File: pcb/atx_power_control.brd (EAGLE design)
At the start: 86 x 70 mm, 57 parts, among them IC2 REG1117, IC3 STM32F042F4, IC4 MY_7905DT, J1 ATX24RH, SW1 324_SW, SW2 324_SW, SW3 324_SW, SW4 324_SW, U2 USBC_16P

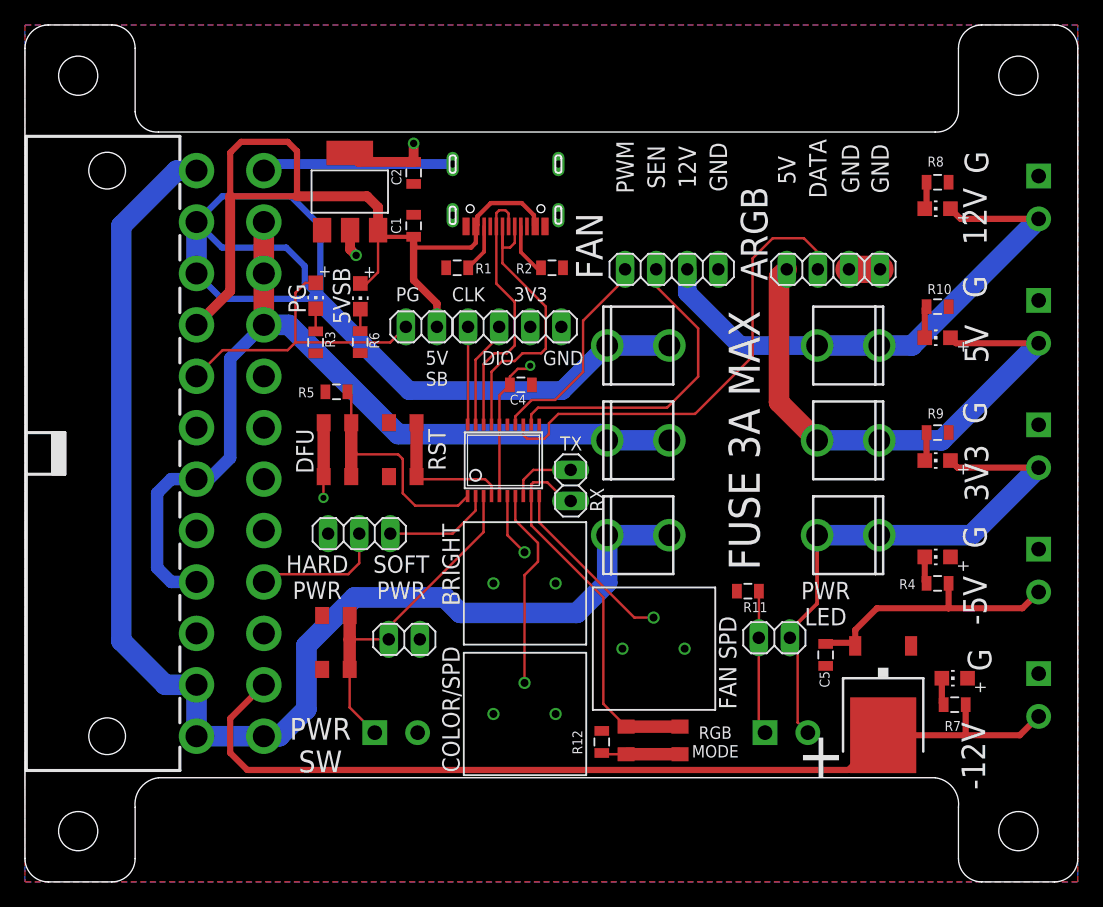
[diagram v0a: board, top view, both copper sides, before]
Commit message: removed pot and added buttons and header
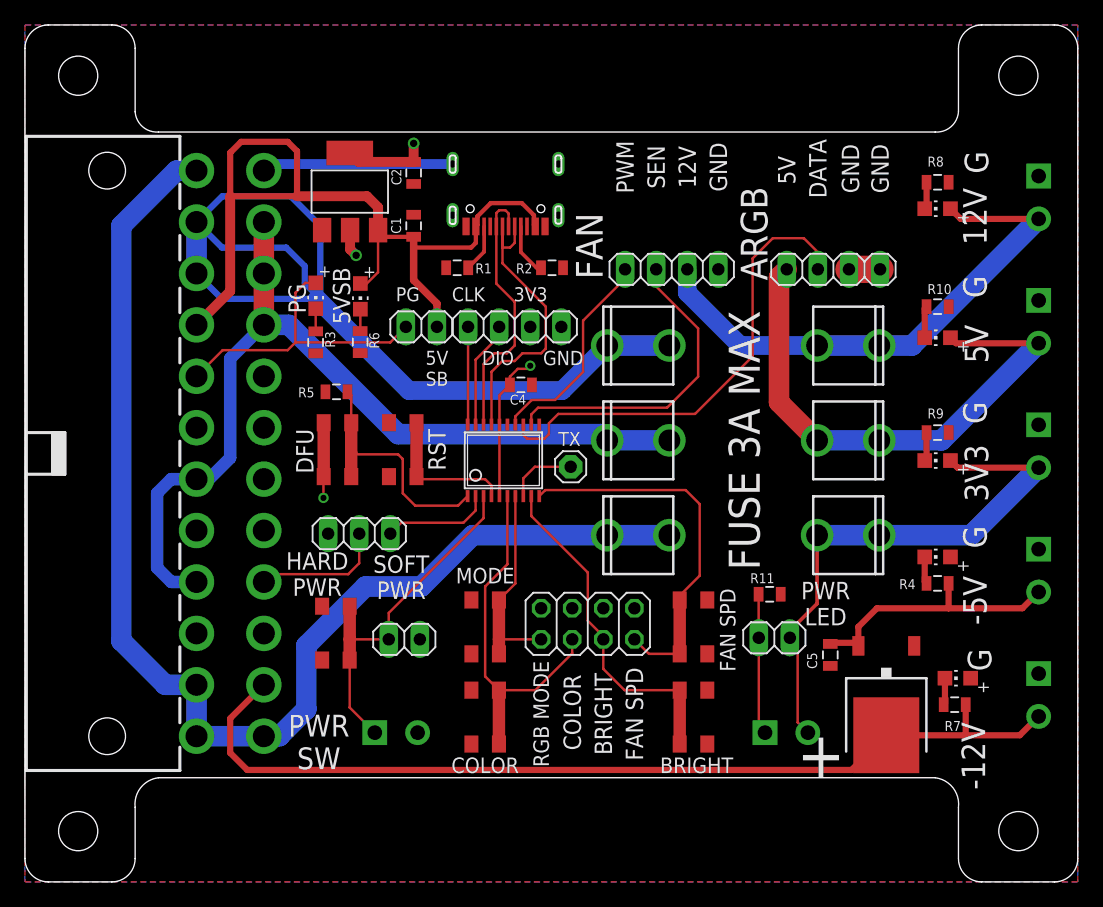
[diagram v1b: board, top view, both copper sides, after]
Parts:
- removed JP4: (no value), pinhead:1X02
- removed R12: 300, joyAnalog:0805
- removed U$4, U$5, U$6: 3386P, bbc_micro:3386P
- added JP10: (no value), adafruit_changed:1X01
- added JP9: (no value), pinhead:2X04
- added SW5, SW6, SW7: 324_SW, 3pos_slide_switch_centered:342_SWICH_FOOT
- moved SW2 13.8 mm to (37.6, 13.5), turned to 90 degrees
- moved R11 1.80 mm to (60.8, 23.5), turned to 180 degrees
- moved SW1 0.76 mm to (25.4, 20.3)
- moved C5 0.38 mm to (65.8, 18.5)
- moved IC4 0.25 mm to (70.4, 14.5)
- moved LED4 0.25 mm to (76.2, 16.6)
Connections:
- removed net N$32: R12.1, SW2.P$2, SW2.P$3
- net +3V3: no longer U$4.B, U$5.B, U$6.B
- net GND: now also JP9.1, JP9.3, JP9.5, JP9.7, SW2.P$2, SW2.P$3, SW5.P$2, SW5.P$3, SW6.P$2, SW6.P$3, SW7.P$2, SW7.P$3; no longer R12.2, U$4.A, U$5.A, U$6.A
- net N$13: now also JP9.6, SW2.P$1, SW2.P$4; no longer U$4.W
- net N$22: now also JP9.8, SW5.P$1, SW5.P$4; no longer U$5.W
- net N$23: now also IC3.8, JP10.1; no longer IC3.10, U$6.W
- net N$27: now also IC3.10, JP9.2, SW7.P$1, SW7.P$4; no longer IC3.8, JP4.2
- net N$30: now also JP9.4, SW6.P$1, SW6.P$4; no longer JP4.1, SW2.P$1, SW2.P$4
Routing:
- net N$27: track 5.53 -> 30.9 mm
- net N$13: track 5.17 -> 29.8 mm
- net N$23: track 14.7 -> 5.71 mm
- net N$32: track 6.43 -> 0.00 mm
- net N$30: track 31.3 -> 27.9 mm
- net N$12: track 105.5 -> 102.2 mm
- net N$26: track 28.5 -> 29.3 mm
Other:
- board text added: "COLOR"
- board text added: "MODE"
- board text removed: "COLOR/SPD"
- board text removed: "RX"

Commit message: updated plate
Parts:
- moved R7 0.40 mm to (76.3, 14.4)
- moved LED4 0.25 mm to (76.5, 16.6)
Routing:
- net GND: track 18.2 -> 29.4 mm
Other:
- board text added: "ATX4VC.COM dekuNukem AUG 2022 PT3"
- board text removed: "ATX CONTROL BOARD dekuNukem AUG 2022 PT3"
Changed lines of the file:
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@@
 <text x="33.655" y="41.9562" size="1.143" layer="25" rot="R180" align="center">5V
 SB</text>
-<text x="6.096" y="35.052" size="2.54" layer="26" rot="MR90" align="center">ATX CONTROL BOARD
+<text x="6.096" y="35.052" size="2.54" layer="26" rot="MR90" align="center">ATX4VC.COM
 dekuNukem AUG 2022
 PT3</text>
@@
 <text x="54.864" y="9.525" size="1.27" layer="25" rot="R180" align="center">BRIGHT</text>
 <text x="57.404" y="20.574" size="1.27" layer="25" rot="R90" align="center">FAN SPD</text>
+<rectangle x1="66.04" y1="8.763" x2="74.549" y2="18.923" layer="41"/>
 </plain>
 <attributes>
@@
 <attribute name="NAME" x="64.7065" y="17.399" size="0.8128" layer="25" rot="R90"/>
 </element>
-<element name="LED4" library="adafruit" package="CHIP-LED0805" value="" x="76.2" y="16.637" smashed="yes" rot="R90">
-<attribute name="VALUE" x="77.47" y="19.177" size="1.27" layer="27" rot="R180"/>
-</element>
-<element name="R7" library="SparkFun-Passives" package="0805" value="5K" x="75.946" y="14.478" smashed="yes" rot="R180">
-<attribute name="NAME" x="76.454" y="13.1445" size="0.8128" layer="25" rot="R180"/>
+<element name="LED4" library="adafruit" package="CHIP-LED0805" value="" x="76.454" y="16.637" smashed="yes" rot="R90">
+<attribute name="VALUE" x="77.724" y="19.177" size="1.27" layer="27" rot="R180"/>
+</element>
+<element name="R7" library="SparkFun-Passives" package="0805" value="5K" x="76.327" y="14.351" smashed="yes" rot="R180">
+<attribute name="NAME" x="76.835" y="13.0175" size="0.8128" layer="25" rot="R180"/>
 </element>
 <element name="LED5" library="adafruit" package="CHIP-LED0805" value="" x="74.549" y="54.991" smashed="yes" rot="R90">
@@
 <contactref element="JP9" pad="5"/>
 <contactref element="JP9" pad="7"/>
+<wire x1="80.3662" y1="19.4558" x2="72.8158" y2="19.4558" width="1.016" layer="1"/>
+<wire x1="72.638" y1="19.278" x2="72.8158" y2="19.4558" width="1.016" layer="1"/>
+<wire x1="80.3662" y1="19.4558" x2="82.804" y2="17.018" width="1.016" layer="1"/>
 </signal>
 <signal name="+3V3">
@@
 <wire x1="16.764" y1="10.541" x2="18.161" y2="9.144" width="0.508" layer="1"/>
 <wire x1="18.161" y1="9.144" x2="67.524" y2="9.144" width="0.508" layer="1"/>
-<wire x1="70.358" y1="11.978" x2="76.835" y2="11.978" width="0.508" layer="1"/>
-<wire x1="76.835" y1="11.978" x2="81.264" y2="11.978" width="0.508" layer="1"/>
+<wire x1="70.358" y1="11.978" x2="77.089" y2="11.978" width="0.508" layer="1"/>
+<wire x1="77.089" y1="11.978" x2="81.264" y2="11.978" width="0.508" layer="1"/>
 <wire x1="81.264" y1="11.978" x2="82.804" y2="13.518" width="0.508" layer="1"/>
-<wire x1="76.846" y1="14.478" x2="76.846" y2="11.989" width="0.508" layer="1"/>
-<wire x1="76.846" y1="11.989" x2="76.835" y2="11.978" width="0.508" layer="1"/>
+<wire x1="77.227" y1="14.351" x2="77.227" y2="12.116" width="0.508" layer="1"/>
+<wire x1="77.227" y1="12.116" x2="77.089" y2="11.978" width="0.508" layer="1"/>
 </signal>
 <signal name="N$11">
@@
 <contactref element="R4" pad="1"/>
 <contactref element="J4" pad="2"/>
-<wire x1="68.078" y1="19.278" x2="68.078" y2="20.834" width="0.508" layer="1"/>
-<wire x1="68.078" y1="20.834" x2="69.596" y2="22.352" width="0.508" layer="1"/>
+<wire x1="68.078" y1="19.278" x2="68.078" y2="20.961" width="0.508" layer="1"/>
+<wire x1="68.078" y1="20.961" x2="69.469" y2="22.352" width="0.508" layer="1"/>
 <wire x1="82.804" y1="23.678" x2="81.478" y2="22.352" width="0.508" layer="1"/>
 <wire x1="81.478" y1="22.352" x2="75.449" y2="22.352" width="0.508" layer="1"/>
-<wire x1="75.449" y1="22.352" x2="69.596" y2="22.352" width="0.508" layer="1"/>
+<wire x1="75.449" y1="22.352" x2="69.469" y2="22.352" width="0.508" layer="1"/>
 <wire x1="75.449" y1="24.384" x2="75.449" y2="22.352" width="0.508" layer="1"/>
 <wire x1="68.078" y1="19.278" x2="67.824" y2="19.532" width="0.508" layer="1"/>
@@
 <contactref element="LED4" pad="C"/>
 <contactref element="R7" pad="2"/>
-<wire x1="75.15" y1="16.637" x2="75.15" y2="14.582" width="0.508" layer="1"/>
-<wire x1="75.046" y1="14.478" x2="75.15" y2="14.582" width="0.508" layer="1"/>
+<wire x1="75.404" y1="16.637" x2="75.404" y2="14.374" width="0.508" layer="1"/>
+<wire x1="75.427" y1="14.351" x2="75.404" y2="14.374" width="0.508" layer="1"/>
 </signal>
 <signal name="N$9">

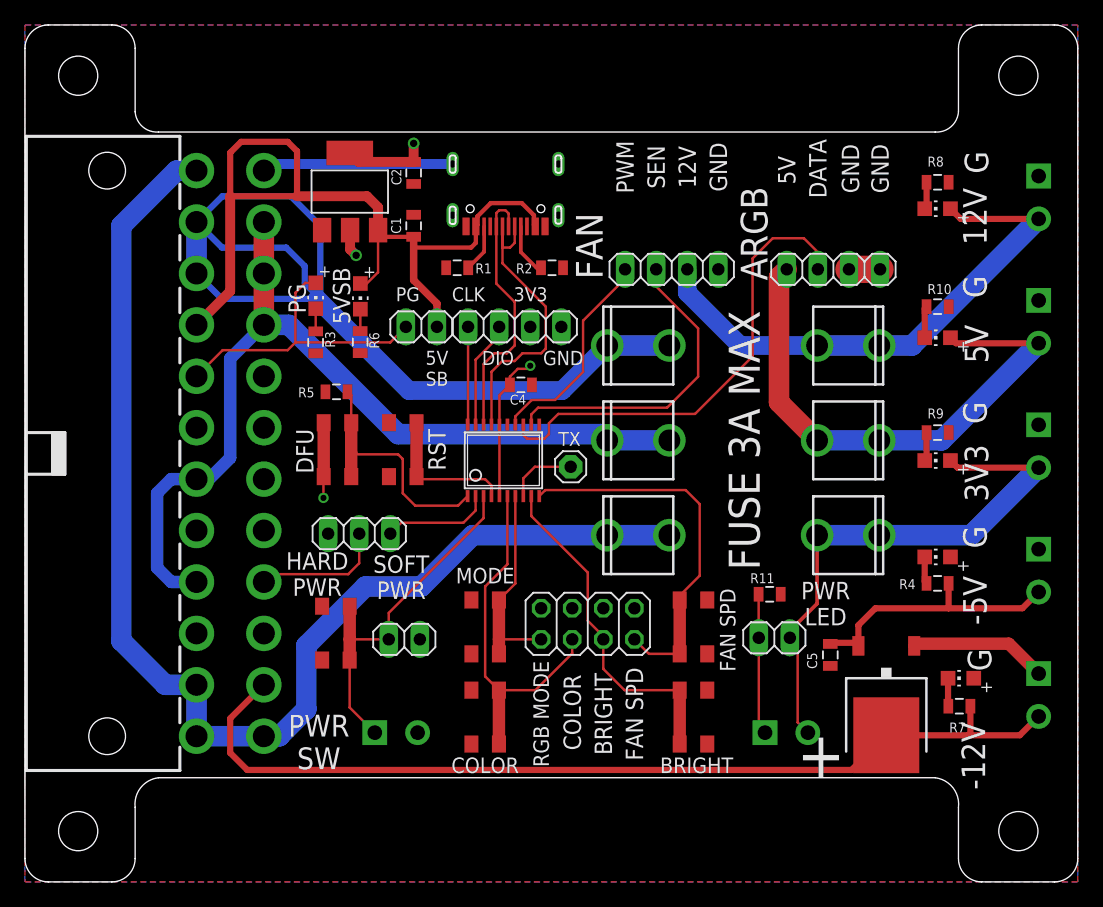
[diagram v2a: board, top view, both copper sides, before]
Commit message: atx rgb done, updated atx psu board too
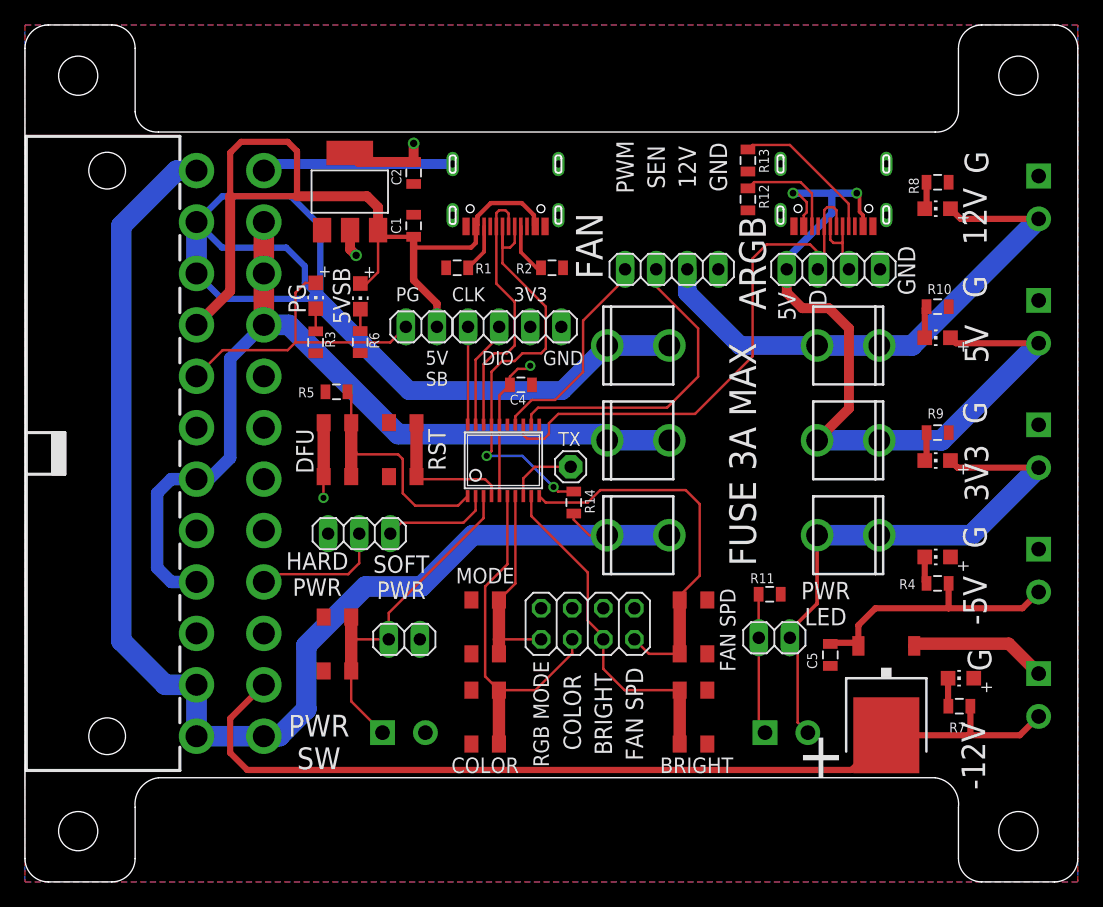
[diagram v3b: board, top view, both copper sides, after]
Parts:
- added R12, R13, R14: 5.1K, joyAnalog:0805
- added U1: USBC_16P, my_usbc_16p:USBC_16P_FOOT
- moved SW1 0.90 mm to (25.5, 19.4)
- moved J5 0.64 mm to (29.2, 12.2)
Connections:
- removed net N$14: IC3.13, JP7.2
- new net N$32: R12.1, U1.B5
- new net N$34: R13.1, U1.A5
- new net N$35: IC3.13, JP7.2, U1.A6, U1.B6
- new net N$36: JP7.3, U1.A7, U1.B7
- net GND: now also R12.2, R13.2, U1.A1B12, U1.B11A12, U1.P$13, U1.P$14, U1.P$15, U1.P$16; no longer JP7.3
- net N$12: now also R14.1
- net N$15: now also U1.A4B9, U1.B4A9
- net USB_DN: now also R14.2
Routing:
- net N$35: track 0.00 -> 46.0 mm
- net N$14: track 38.9 -> 0.00 mm
- net N$15: track 44.3 -> 66.6 mm, vias 0 -> 2
- net N$34: track 0.00 -> 12.2 mm
- net USB_DN: track 25.2 -> 36.2 mm, vias 0 -> 2
- net N$32: track 0.00 -> 8.51 mm
- net N$36: track 0.00 -> 5.95 mm
- net N$12: track 102.2 -> 106.0 mm
- net GND: track 29.4 -> 26.9 mm
- net N$26: track 29.3 -> 28.5 mm
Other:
- board text added: "ATX4VC.COM dekuNukem SEPT 2022 PT3"
- board text added: "D"
- board text removed: "ATX4VC.COM dekuNukem AUG 2022 PT3"
- board text removed: "DATA"
